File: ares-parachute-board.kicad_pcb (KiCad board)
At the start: 2 copper layers, 57 x 88 mm, 236 parts, among them J1 Conn_01x16_Female, J3 Conn_01x02_Male, J4 Conn_ARM_JTAG_SWD_10, J5 Conn_01x03_Pin, J6 MPT 0.5/2-2.54, T1 RH-5000, T2 RH-5000, T3 RH-5000, T4 RH-5000, T5 RH-5000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

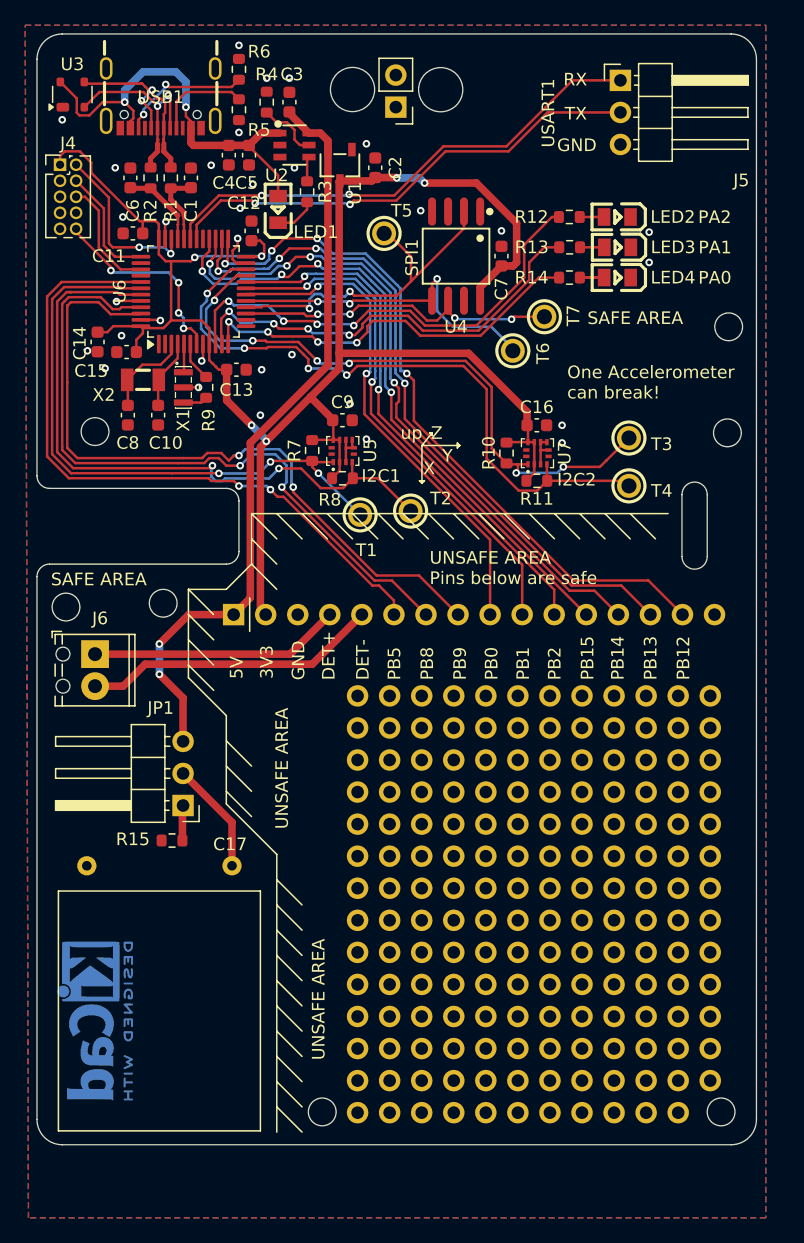
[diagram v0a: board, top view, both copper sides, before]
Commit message: update board for prototype 2
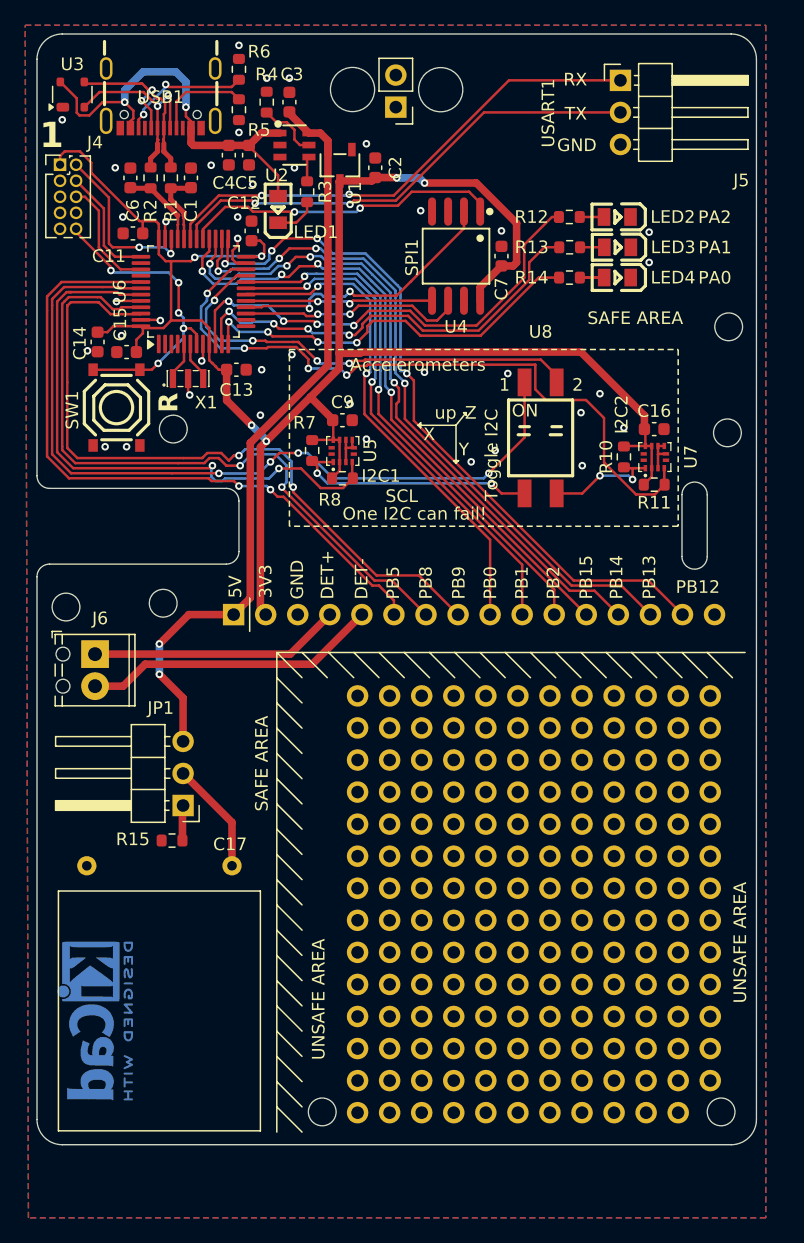
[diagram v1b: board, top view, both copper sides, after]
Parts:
- removed C10, C8: 12.5p, Capacitor_SMD:C_0603_1608Metric
- removed R9: 0, Resistor_SMD:R_0603_1608Metric
- removed T1, T2, T3, T4, T5, T6, T7: RH-5000, easyeda_exported:TEST-TH_BD2.54-P1.4_RED
- removed X2: Q13FC1350000400, easyeda_exported:FC-135R_L3.2-W1.5
- added SW1: TS-1187A-B-A-B, easyeda_exported:SW-SMD_4P-L5.1-W5.1-P3.70-LS6.5-TL_H1.5, F.Cu at (186.3, 81.6)
- added U8: DSIC-02-TS-GER, easyeda_exported:SW-SMD_DSIC-02-TS-GER, F.Cu at (219.9, 84.0)
- R12, R13: value 270 -> 560
- R14: value 100 -> 2k2
- R5, R6: value 5.1k -> 5k1
- moved R10 9.31 mm to (226.5, 85.5)
- moved U7 9.31 mm to (229.0, 85.5)
- moved R11 9.30 mm to (228.9, 87.7)
- moved C16 9.30 mm to (228.9, 83.3)
- moved REF** 6.20 mm to (190.8, 83.3)
- moved X1 0.79 mm to (192.0, 79.3), turned to 0 degrees
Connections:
- R10 pad 2: /I2C2_SCL -> /I2C2_SCL_DC
- R7 pad 2: /I2C1_SCL -> /I2C1_SCL_DC
- U5 pad 1: /I2C1_SCL -> /I2C1_SCL_DC
- U6 pad 29: unconnected-(U6-PA8-Pad29) -> /~{MEM_CS}
- U6 pad 3: Net-(U6-PC14) -> unconnected-(U6-PC14-Pad3)
- U6 pad 4: Net-(U6-PC15) -> unconnected-(U6-PC15-Pad4)
- U7 pad 1: /I2C2_SCL -> /I2C2_SCL_DC
- X1 pad 3: Net-(R9-Pad1) -> Net-(U6-PD1)
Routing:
- net /~{MEM_CS}: track 0.00 -> 25.3 mm, vias 0 -> 2
- net /I2C1_SCL_DC: track 0.00 -> 19.9 mm, vias 0 -> 2
- net /I2C1_SCL: track 49.0 -> 65.0 mm, vias 3 -> 4
- net /I2C2_SCL: track 49.7 -> 36.0 mm, vias 6 -> 4
- net /SPI1_MOSI: track 26.8 -> 14.9 mm, vias 3 -> 2
- net +3.3V: track 149.5 -> 159.0 mm
- net /I2C2_SCL_DC: track 0.00 -> 9.35 mm, vias 0 -> 2
- net /~{RESET}: track 16.0 -> 25.0 mm, vias 4 -> 5
- net /SPI1_SCK: track 26.8 -> 18.8 mm, vias 4 -> 2
- net Net-(U6-PC14): track 7.18 -> 0.00 mm
- net /I2C1_SDA: track 52.7 -> 47.0 mm
- net Net-(U6-PC15): track 5.50 -> 0.00 mm
- net /SPI1_MISO: track 27.1 -> 22.2 mm
- net /I2C2_SDA: track 52.2 -> 55.1 mm
- net Net-(R9-Pad1): track 1.96 -> 0.00 mm
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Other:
- board text added: "1"
- board text added: "ARES Parachute Board PROTO2 (c) 2025 Hochschule Luzern, Technik & Architektur"
- board text added: "Accelerometers"
- board text added: "One I2C can fail!"
- board text added: "R"
- board text added: "SCL"
- board text added: "Toggle I2C"
- board text removed: "ARES Parachute Board PROTO1 (c) 2024 Hochschule Luzern, Technik & Architektur"
- board text removed: "One Accelerometer can break!"
- board text removed: "Power Stuff"
- board text removed: "UNSAFE AREA Pins below are safe"

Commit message: ordered version 1.0
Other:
- board text added: "ARES Parachute Board v1.0 (c) 2025 Hochschule Luzern, Technik & Architektur"
- board text added: "CS PA8"
- board text removed: "ARES Parachute Board PROTO2 (c) 2025 Hochschule Luzern, Technik & Architektur"
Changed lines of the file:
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@@
 		(sheetname "Root")
 		(sheetfile "ares-parachute-board.kicad_sch")
-		(attr through_hole exclude_from_pos_files)
+		(attr through_hole exclude_from_pos_files exclude_from_bom)
 		(fp_line
 			(start -1.33 1.27)
@@
 		(sheetname "Root")
 		(sheetfile "ares-parachute-board.kicad_sch")
-		(attr through_hole exclude_from_pos_files)
+		(attr through_hole exclude_from_pos_files exclude_from_bom)
 		(fp_line
 			(start 1.33 1.27)
@@
 		(sheetname "Root")
 		(sheetfile "ares-parachute-board.kicad_sch")
-		(attr through_hole exclude_from_pos_files)
+		(attr through_hole exclude_from_pos_files exclude_from_bom)
 		(fp_line
 			(start -1.27 -1.27)
@@
 		(at 191.970006 79.299992)
 		(property "Reference" "X1"
-			(at 1.43 1.9 360)
+			(at 1.43 1.9 0)
 			(layer "F.SilkS")
 			(effects
@@
 		)
 		(property "Value" "CSTNE8M00G520000R0"
-			(at 0 4 360)
+			(at 0 4 0)
 			(layer "F.Fab")
 			(effects
@@
 		)
 		(property "Footprint" "easyeda_exported:OSC-SMD_3P-L3.2-W1.3-P1.20"
-			(at 0 0 360)
+			(at 0 0 0)
 			(layer "F.Fab")
 			(hide yes)
@@
 		)
 		(property "Datasheet" ""
-			(at 0 0 360)
+			(at 0 0 0)
 			(layer "F.Fab")
 			(hide yes)
@@
 		)
 		(property "Description" ""
-			(at 0 0 360)
+			(at 0 0 0)
 			(layer "F.Fab")
 			(hide yes)
@@
 		)
 		(fp_text user "${REFERENCE}"
-			(at 0 0 360)
+			(at 0 0 0)
 			(layer "F.Fab")
 			(effects
@@
 			)
 		)
-		(property "LCSC" "C22966"
+		(property "LCSC" "C23204"
 			(at 0 0 0)
 			(layer "F.SilkS")
@@
 		(sheetname "Root")
 		(sheetfile "ares-parachute-board.kicad_sch")
-		(attr through_hole exclude_from_pos_files)
+		(attr through_hole exclude_from_pos_files exclude_from_bom)
 		(fp_line
 			(start -1.8 3.4)
@@
 		(at 219.900006 83.999992)
 		(property "Reference" "U8"
-			(at 0 -8.4 360)
+			(at 0 -8.4 0)
 			(layer "F.SilkS")
 			(effects
@@
 		)
 		(property "Value" "DSIC-02-TS-GER"
-			(at 0 8.4 360)
+			(at 0 8.4 0)
 			(layer "F.Fab")
 			(effects
@@
 		)
 		(property "Footprint" "easyeda_exported:SW-SMD_DSIC-02-TS-GER"
-			(at 0 0 360)
+			(at 0 0 0)
 			(layer "F.Fab")
 			(hide yes)
@@
 		)
 		(property "Datasheet" ""
-			(at 0 0 360)
+			(at 0 0 0)
 			(layer "F.Fab")
 			(hide yes)
@@
 		)
 		(property "Description" ""
-			(at 0 0 360)
+			(at 0 0 0)
 			(layer "F.Fab")
 			(hide yes)
@@
 		)
 		(fp_text user "1"
-			(at -3.3 -4.2 360)
+			(at -3.3 -4.2 0)
 			(layer "F.SilkS")
 			(effects
@@
 		)
 		(fp_text user "2"
-			(at 2.5 -4.2 360)
+			(at 2.5 -4.2 0)
 			(layer "F.SilkS")
 			(effects
@@
 		)
 		(fp_text user "ON"
-			(at -2.29 -2.16 360)
+			(at -2.29 -2.16 0)
 			(layer "F.SilkS")
 			(effects
@@
 		)
 		(fp_text user "${REFERENCE}"
-			(at 0 0 360)
+			(at 0 0 0)
 			(layer "F.Fab")
 			(effects
@@
 			)
 		)
-		(property "LCSC" "C22775"
+		(property "LCSC" "C4190"
 			(at 0 0 0)
 			(layer "F.SilkS")
@@
 			)
 		)
-		(property "LCSC" "C22966"
+		(property "LCSC" "C23204"
 			(at 0 0 0)
 			(layer "F.SilkS")
@@
 		(sheetname "Root")
 		(sheetfile "ares-parachute-board.kicad_sch")
-		(attr through_hole exclude_from_pos_files)
+		(attr through_hole exclude_from_pos_files exclude_from_bom)
 		(fp_line
 			(start -2 -13.75)
@@
 		(layer "Edge.Cuts")
 	)
-	(gr_text "ARES Parachute Board PROTO2\n(c) 2025 Hochschule Luzern, Technik & Architektur"
+	(gr_text "ARES Parachute Board v1.0\n(c) 2025 Hochschule Luzern, Technik & Architektur"
 		(at 188.100006 97.999992 90)
 		(layer "B.SilkS")
@@
 			)
 			(justify left bottom)
+		)
+	)
+	(gr_text "CS PA8"
+		(at 209.000006 72.399992 90)
+		(layer "F.SilkS")
+		(effects
+			(font
+				(size 1 1)
+				(thickness 0.15)
+			)
+			(justify left bottom)

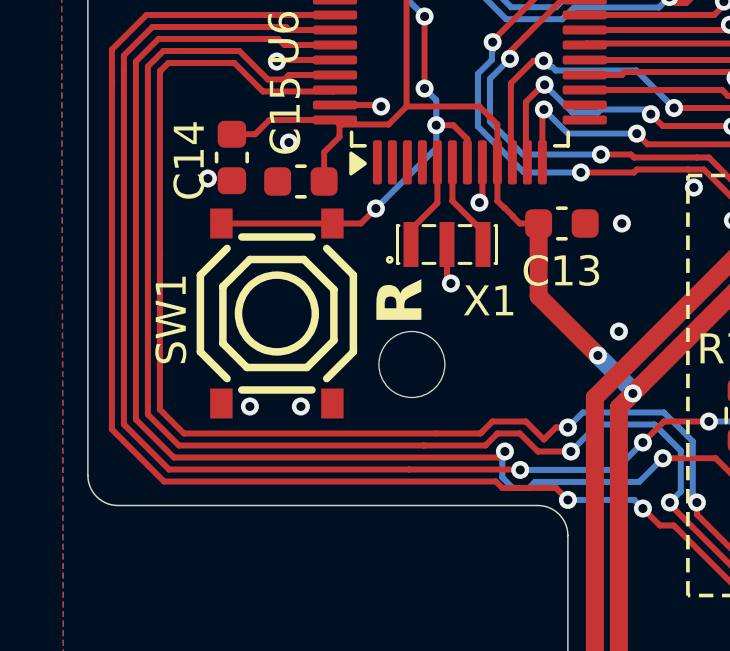
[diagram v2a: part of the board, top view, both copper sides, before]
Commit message: fix error in reset button placement for future revision
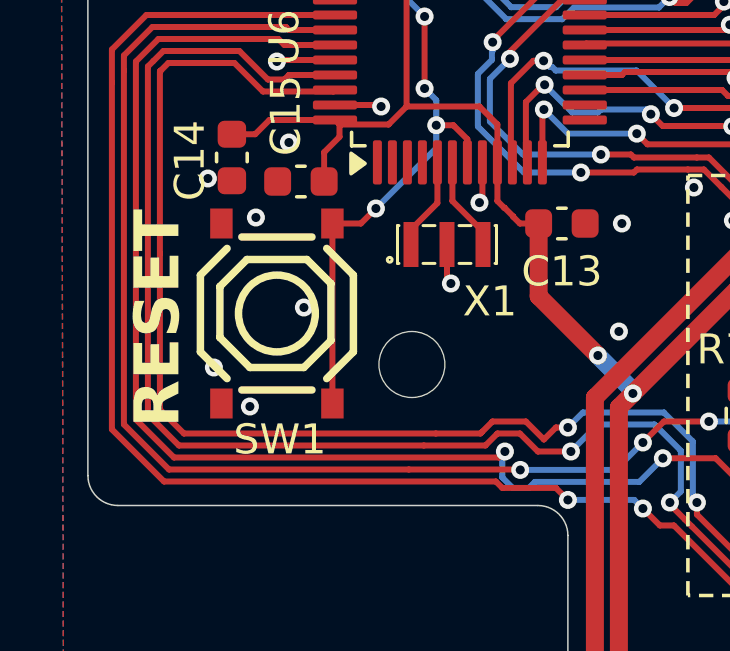
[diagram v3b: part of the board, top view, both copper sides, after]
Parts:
- turned SW1 to -90 degrees
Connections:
- SW1 pad 1: GND -> /~{RESET}
- SW1 pad 4: /~{RESET} -> GND
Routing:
- net /~{RESET}: track 25.0 -> 27.3 mm
- net GND: vias 39 -> 41
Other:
- board text added: "ARES Parachute Board v1.1 (c) 2025 Hochschule Luzern, Technik & Architektur"
- board text added: "RESET"
- board text removed: "ARES Parachute Board v1.0 (c) 2025 Hochschule Luzern, Technik & Architektur"
- board text removed: "R"
